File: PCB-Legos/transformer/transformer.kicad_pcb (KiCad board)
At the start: 4 copper layers, 21.8 x 9.7 mm, 3 parts, among them J1 Conn_Coaxial, U1 NCS3-272+

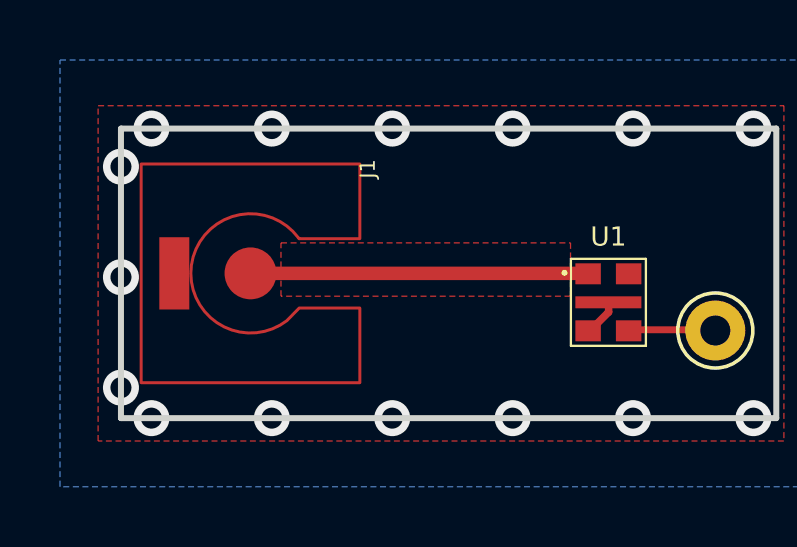
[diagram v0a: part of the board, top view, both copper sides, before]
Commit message: sweaks to sma connector footprint to unbork the errors from the eagle port
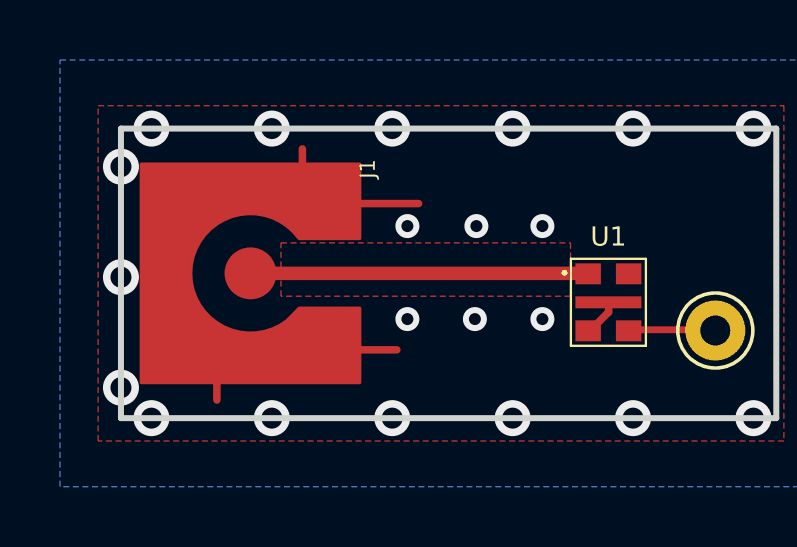
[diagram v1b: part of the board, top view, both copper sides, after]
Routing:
- net GND: track 1.74 -> 10.3 mm, vias 15 -> 21
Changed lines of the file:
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@@
         (xy -3.6449 -3.6449)
         (xy -1.1557 -3.6449)
-      ) (layer "F.Cu") (width 0.1) (fill none))
+      ) (layer "F.Cu") (width 0.1) (fill solid))
     (fp_poly (pts
-        (xy 1.4478 -1.4478)
-        (xy 3.302 -1.4478)
-        (xy 3.302 -3.302)
-        (xy 1.4478 -3.302)
-      ) (layer "F.Paste") (width 0.1) (fill none))
+        (xy -3.81 3.81)
+        (xy -1.205 3.81)
+        (xy -1.27 -3.81)
+        (xy -3.81 -3.81)
+      ) (layer "F.Mask") (width 0.1) (fill solid))
     (fp_poly (pts
-        (xy 1.4478 3.302)
-        (xy 3.302 3.302)
-        (xy 3.302 1.4478)
-        (xy 1.4478 1.4478)
-      ) (layer "F.Paste") (width 0.1) (fill none))
-    (fp_poly (pts
-        (xy -3.302 3.302)
-        (xy -1.4478 3.302)
-        (xy -1.4478 1.4478)
-        (xy -3.302 1.4478)
-      ) (layer "F.Paste") (width 0.1) (fill none))
-    (fp_poly (pts
-        (xy -3.302 -1.4478)
-        (xy -1.4478 -1.4478)
-        (xy -1.4478 -3.302)
-        (xy -3.302 -3.302)
-      ) (layer "F.Paste") (width 0.1) (fill none))
-    (fp_poly (pts
-        (xy -3.429 -0.762)
-        (xy -0.635 -0.762)
-        (xy -0.635 -1.143)
-        (xy -3.429 -1.143)
-      ) (layer "F.Mask") (width 0.1) (fill none))
-    (fp_poly (pts
-        (xy 0.635 -0.762)
-        (xy 3.429 -0.762)
-        (xy 3.429 -1.143)
-        (xy 0.635 -1.143)
-      ) (layer "F.Mask") (width 0.1) (fill none))
-    (fp_poly (pts
-        (xy -3.429 3.429)
-        (xy 3.429 3.429)
-        (xy 3.429 -0.889)
-        (xy -3.429 -0.889)
-      ) (layer "F.Mask") (width 0.1) (fill none))
-    (fp_poly (pts
-        (xy -3.429 -1.016)
-        (xy 3.429 -1.016)
-        (xy 3.429 -3.429)
-        (xy -3.429 -3.429)
-      ) (layer "F.Mask") (width 0.1) (fill none))
-    (fp_poly (pts
-        (xy 0.635 -0.762)
-        (xy 3.429 -0.762)
-        (xy 3.429 -1.143)
-        (xy 0.635 -1.143)
-      ) (layer "F.Mask") (width 0.1) (fill none))
+        (xy 1.27 3.81)
+        (xy 3.81 3.81)
+        (xy 3.81 -3.81)
+        (xy 1.27 -3.81)
+      ) (layer "F.Mask") (width 0.1) (fill solid))
     (fp_line (start -4.1 4.1) (end -4.1 -4.1) (layer "F.CrtYd") (width 0.05))
     (fp_line (start 4.1 -4.1) (end 4.1 4.1) (layer "F.CrtYd") (width 0.05))
@@
     (pad "CENTER" smd roundrect (at 0 0 270) (size 1.73 1.73) (layers "F.Cu" "F.Paste") (roundrect_rratio 0.5)
       (net 1 "Net-(J1-Pad1)") (solder_mask_margin 0.0635))
-    (pad "SHIELD" smd rect (at 0 2.54 270) (size 2.41 1) (layers "F.Cu" "F.Paste" "F.Mask")
-      (net 2 "GND") (solder_mask_margin 0.0635))
   )
   (gr_poly
     (pts
-      (xy 113.538 50.038)
-      (xy 103.886 50.038)
-      (xy 103.886 48.768)
-      (xy 113.538 48.768)
-    ) (layer "F.Mask") (width 0) (fill none))
+      (xy 113.613 50.045)
+      (xy 103.886 50.045)
+      (xy 103.886 48.5)
+      (xy 113.613 48.5)
+    ) (layer "F.Mask") (width 0.1) (fill solid))
   (gr_rect (start 120.396 44.45) (end 98.552 54.102) (layer "Edge.Cuts") (width 0.2) (fill none))
   (segment (start 114.067 49.276) (end 114.133 49.342) (width 0.25) (layer "F.Cu") (net 1))
   (segment (start 103.212 49.276) (end 114.212 49.276) (width 0.45) (layer "F.Cu") (net 1))
   (segment (start 114.808 50.292) (end 114.3 50.292) (width 0.25) (layer "F.Cu") (net 2))
+  (segment (start 101.75 52.025) (end 101.75 53.5) (width 0.25) (layer "F.Cu") (net 2))
   (segment (start 114.808 50.567) (end 114.133 51.242) (width 0.25) (layer "F.Cu") (net 2))
   (segment (start 114.808 50.292) (end 114.808 50.567) (width 0.25) (layer "F.Cu") (net 2))
+  (segment (start 104.6 46.375) (end 104.6 45.125) (width 0.25) (layer "F.Cu") (net 2))
+  (segment (start 105.325 51.825) (end 105.3 51.8) (width 0.25) (layer "F.Cu") (net 2))
+  (segment (start 107.75 51.825) (end 105.325 51.825) (width 0.25) (layer "F.Cu") (net 2))
+  (segment (start 108.475 46.95) (end 105.1 46.95) (width 0.25) (layer "F.Cu") (net 2))
   (via (at 115.6208 54.102) (size 1.2) (drill 0.7) (layers "F.Cu" "B.Cu") (free) (net 2))
+  (via (at 112.6 50.8) (size 0.8) (drill 0.4) (layers "F.Cu" "B.Cu") (free) (net 2))
+  (via (at 112.6 47.7) (size 0.8) (drill 0.4) (layers "F.Cu" "B.Cu") (free) (net 2))
   (via (at 98.552 53.086) (size 1.2) (drill 0.7) (layers "F.Cu" "B.Cu") (free) (net 2))
   (via (at 107.5944 44.45) (size 1.2) (drill 0.7) (layers "F.Cu" "B.Cu") (free) (net 2))
   (via (at 107.5944 54.102) (size 1.2) (drill 0.7) (layers "F.Cu" "B.Cu") (free) (net 2))
   (via (at 111.6076 44.45) (size 1.2) (drill 0.7) (layers "F.Cu" "B.Cu") (free) (net 2))
+  (via (at 108.1 47.7) (size 0.8) (drill 0.4) (layers "F.Cu" "B.Cu") (free) (net 2))
   (via (at 119.634 54.102) (size 1.2) (drill 0.7) (layers "F.Cu" "B.Cu") (free) (net 2))
+  (via (at 108.1 50.8) (size 0.8) (drill 0.4) (layers "F.Cu" "B.Cu") (free) (net 2))
   (via (at 103.5812 44.45) (size 1.2) (drill 0.7) (layers "F.Cu" "B.Cu") (free) (net 2))
   (via (at 99.568 54.102) (size 1.2) (drill 0.7) (layers "F.Cu" "B.Cu") (free) (net 2))
   (via (at 103.5812 54.102) (size 1.2) (drill 0.7) (layers "F.Cu" "B.Cu") (free) (net 2))
+  (via (at 110.35 50.8) (size 0.8) (drill 0.4) (layers "F.Cu" "B.Cu") (free) (net 2))
   (via (at 115.6208 44.45) (size 1.2) (drill 0.7) (layers "F.Cu" "B.Cu") (free) (net 2))
   (via (at 111.6076 54.102) (size 1.2) (drill 0.7) (layers "F.Cu" "B.Cu") (free) (net 2))
@@
   (via (at 98.552 45.72) (size 1.2) (drill 0.7) (layers "F.Cu" "B.Cu") (free) (net 2))
   (via (at 99.568 44.45) (size 1.2) (drill 0.7) (layers "F.Cu" "B.Cu") (net 2))
+  (via (at 110.4 47.7) (size 0.8) (drill 0.4) (layers "F.Cu" "B.Cu") (free) (net 2))
   (segment (start 115.4833 51.1556) (end 118.2983 51.1556) (width 0.23) (layer "F.Cu") (net 3))
   (segment (start 118.298 51.242) (end 118.364 51.308) (width 0.25) (layer "F.Cu") (net 3))

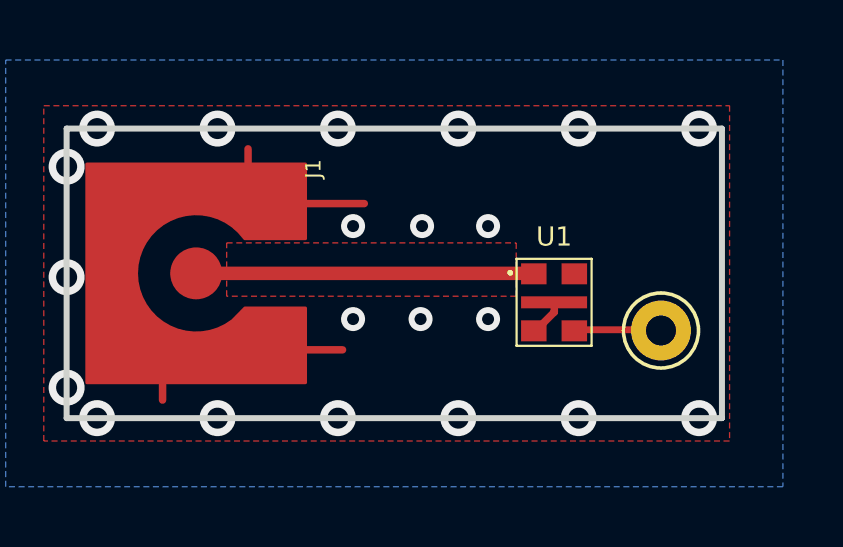
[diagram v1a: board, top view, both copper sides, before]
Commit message: Fixed .gitignore for KiCAD 6, removed backups and other temp files, updated board file with 4 layer oshpark from the oresat-kicad repo, moved antenna much closer to the transformer and reduced the trace size to minimum (as close to 150 ohms as possible), and set net classes to RF-50-MAX which gives lots of ground clearance.
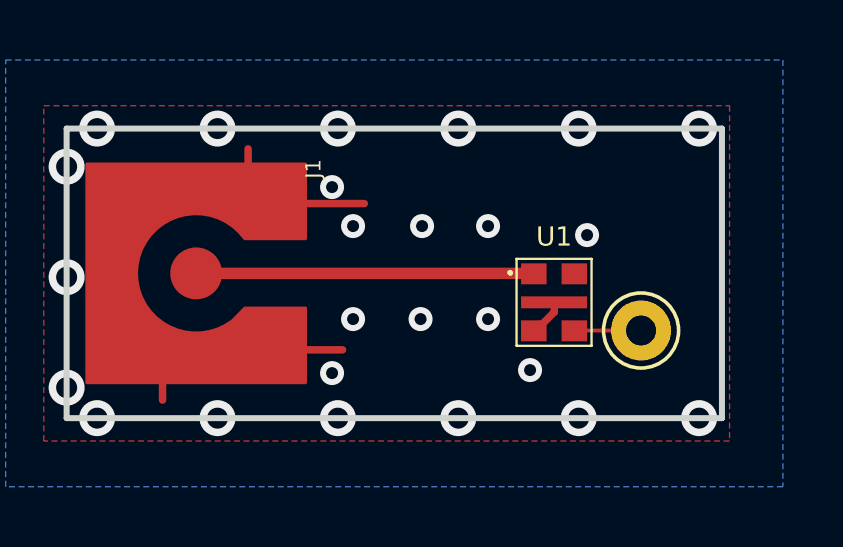
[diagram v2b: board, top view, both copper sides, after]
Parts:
- moved H1 0.66 mm to (117.7, 51.2)
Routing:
- net Net-(H1-Pad1): track 2.91 -> 2.32 mm
- net GND: vias 21 -> 25
- removed copper zone on F.Cu, net (none)
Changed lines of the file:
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@@
   (paper "A4")
   (layers
-    (0 "F.Cu" signal)
+    (0 "F.Cu" jumper)
     (1 "In1.Cu" signal)
     (2 "In2.Cu" signal)
     (31 "B.Cu" signal)
-    (32 "B.Adhes" user "B.Adhesive")
-    (33 "F.Adhes" user "F.Adhesive")
     (34 "B.Paste" user)
     (35 "F.Paste" user)
@@
     (40 "Dwgs.User" user "User.Drawings")
     (41 "Cmts.User" user "User.Comments")
-    (42 "Eco1.User" user "User.Eco1")
-    (43 "Eco2.User" user "User.Eco2")
     (44 "Edge.Cuts" user)
     (45 "Margin" user)
@@
     (48 "B.Fab" user)
     (49 "F.Fab" user)
-    (50 "User.1" user)
-    (51 "User.2" user)
-    (52 "User.3" user)
-    (53 "User.4" user)
-    (54 "User.5" user)
-    (55 "User.6" user)
-    (56 "User.7" user)
-    (57 "User.8" user)
-    (58 "User.9" user)
   )
   (setup
@@
     )
     (pad_to_mask_clearance 0)
+    (solder_mask_min_width 0.1016)
     (pcbplotparams
       (layerselection 0x00010fc_ffffffff)
@@
   (net 3 "Net-(H1-Pad1)")
   (footprint "Connector_Pin:Pin_D1.0mm_L10.0mm" (layer "F.Cu")
-    (at 118.364 51.181)
+    (at 117.7 51.181)
     (descr "solder Pin_ diameter 1.0mm, hole diameter 1.0mm (press fit), length 10.0mm")
     (tags "solder Pin_ press fit")
@@
       (net 1 "Net-(J1-Pad1)") (solder_mask_margin 0.0635))
   )
-  (gr_poly
-    (pts
-      (xy 113.613 50.045)
-      (xy 103.886 50.045)
-      (xy 103.886 48.5)
-      (xy 113.613 48.5)
-    ) (layer "F.Mask") (width 0.1) (fill solid))
   (gr_rect (start 120.396 44.45) (end 98.552 54.102) (layer "Edge.Cuts") (width 0.2) (fill none))
   (segment (start 114.067 49.276) (end 114.133 49.342) (width 0.25) (layer "F.Cu") (net 1))
-  (segment (start 103.212 49.276) (end 114.212 49.276) (width 0.45) (layer "F.Cu") (net 1))
+  (segment (start 103.212 49.276) (end 114.212 49.276) (width 0.38) (layer "F.Cu") (net 1))
   (segment (start 114.808 50.292) (end 114.3 50.292) (width 0.25) (layer "F.Cu") (net 2))
   (segment (start 101.75 52.025) (end 101.75 53.5) (width 0.25) (layer "F.Cu") (net 2))
@@
   (segment (start 107.75 51.825) (end 105.325 51.825) (width 0.25) (layer "F.Cu") (net 2))
   (segment (start 108.475 46.95) (end 105.1 46.95) (width 0.25) (layer "F.Cu") (net 2))
+  (via (at 114 52.5) (size 0.8) (drill 0.4) (layers "F.Cu" "B.Cu") (free) (net 2))
+  (via (at 115.9 48) (size 0.8) (drill 0.4) (layers "F.Cu" "B.Cu") (free) (net 2))
+  (via (at 107.4 46.4) (size 0.8) (drill 0.4) (layers "F.Cu" "B.Cu") (free) (net 2))
   (via (at 115.6208 54.102) (size 1.2) (drill 0.7) (layers "F.Cu" "B.Cu") (free) (net 2))
   (via (at 112.6 50.8) (size 0.8) (drill 0.4) (layers "F.Cu" "B.Cu") (free) (net 2))
@@
   (via (at 111.6076 44.45) (size 1.2) (drill 0.7) (layers "F.Cu" "B.Cu") (free) (net 2))
   (via (at 108.1 47.7) (size 0.8) (drill 0.4) (layers "F.Cu" "B.Cu") (free) (net 2))
+  (via (at 107.4 52.6) (size 0.8) (drill 0.4) (layers "F.Cu" "B.Cu") (free) (net 2))
   (via (at 119.634 54.102) (size 1.2) (drill 0.7) (layers "F.Cu" "B.Cu") (free) (net 2))
   (via (at 108.1 50.8) (size 0.8) (drill 0.4) (layers "F.Cu" "B.Cu") (free) (net 2))
@@
   (via (at 99.568 44.45) (size 1.2) (drill 0.7) (layers "F.Cu" "B.Cu") (net 2))
   (via (at 110.4 47.7) (size 0.8) (drill 0.4) (layers "F.Cu" "B.Cu") (free) (net 2))
-  (segment (start 115.4833 51.1556) (end 118.2983 51.1556) (width 0.23) (layer "F.Cu") (net 3))
+  (segment (start 115.4851 51.181) (end 115.4749 51.1912) (width 0.127) (layer "F.Cu") (net 3))
   (segment (start 118.298 51.242) (end 118.364 51.308) (width 0.25) (layer "F.Cu") (net 3))
-  (zone (net 0) (net_name "") (layer "F.Cu") (hatch edge 0.508)
-    (connect_pads (clearance 0.381))
-    (min_thickness 0.254) (filled_areas_thickness no)
-    (fill yes (thermal_gap 0.508) (thermal_bridge_width 0.508))
-    (polygon
-      (pts
-        (xy 113.538 50.038)
-        (xy 103.886 50.038)
-        (xy 103.886 48.26)
-        (xy 113.538 48.26)
-      )
-    )
-  )
+  (segment (start 117.7 51.181) (end 115.4851 51.181) (width 0.127) (layer "F.Cu") (net 3))
   (zone (net 2) (net_name "GND") (layer "F.Cu") (hatch edge 0.508)
     (connect_pads (clearance 0.381))
@@
       )
     )
+  )
+  (zone (net 0) (net_name "") (layer "F.Mask") (hatch full 0.508)
+    (connect_pads (clearance 0.381))
+    (min_thickness 0.127) (filled_areas_thickness no)
+    (fill yes (thermal_gap 0.508) (thermal_bridge_width 0.508))
+    (polygon
+      (pts
+        (xy 113.4 50.3)
+        (xy 103.9 50.3)
+        (xy 103.9 48.2)
+        (xy 113.4 48.2)
+      )
+    )

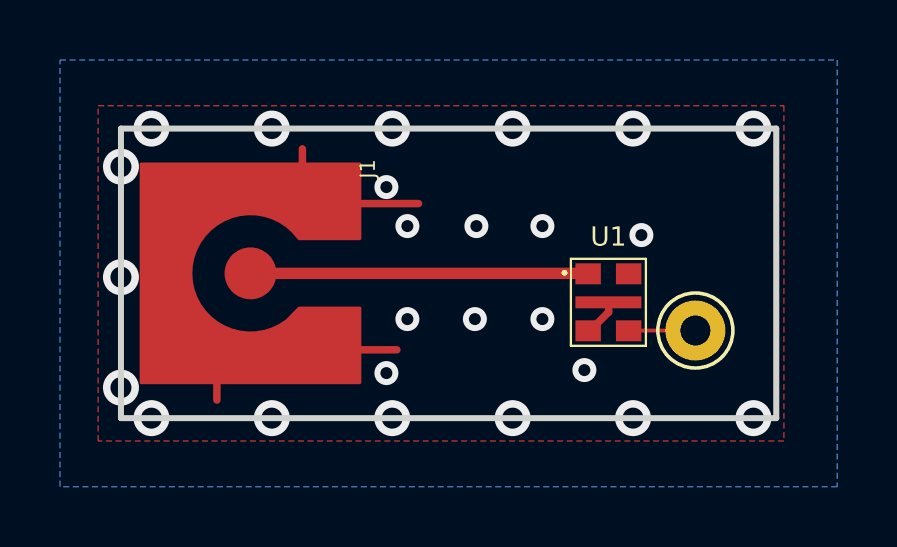
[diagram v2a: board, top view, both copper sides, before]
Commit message: fixed SMA connector footprint, moved text from paste to silk layer
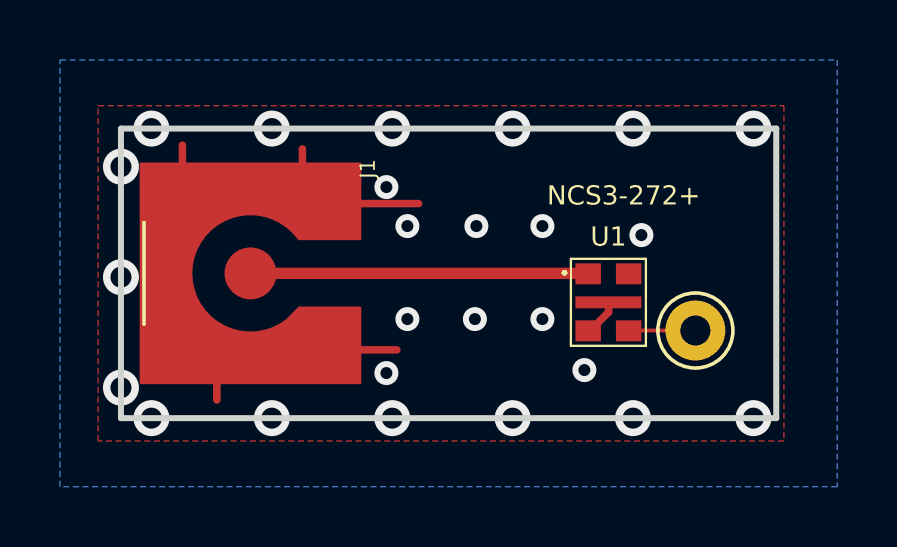
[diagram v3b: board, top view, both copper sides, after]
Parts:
- J1: footprint HGS_Reflector:132134-10 -> Footprints:J-Amphenol-132134-10-SMA-F-SMT-vertical
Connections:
- J1 pad CENTER: Net-(J1-Pad1) -> (no net)
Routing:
- net (no net): track 0.00 -> 0.90 mm
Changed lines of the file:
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@@
       (effects (font (size 0.640777 0.640777) (thickness 0.15)))
     )
-    (fp_text value "NCS3-272+" (at 0.508 -3.556) (layer "F.Paste")
+    (fp_text value "NCS3-272+" (at 0.508 -3.556) (layer "F.SilkS")
       (effects (font (size 0.640436 0.640436) (thickness 0.15)))
     )
@@
     (pad "6" smd rect locked (at 0.675 -0.95) (size 0.85 0.7) (layers "F.Cu" "F.Paste" "F.Mask"))
   )
-  (footprint "HGS_Reflector:132134-10" (layer "F.Cu")
+  (footprint "Footprints:J-Amphenol-132134-10-SMA-F-SMT-vertical" (layer "F.Cu")
     (at 102.87 49.276 -90)
     (property "Sheetfile" "transformer.kicad_sch")
@@
       ) (layer "F.Cu") (width 0.1) (fill solid))
     (fp_poly (pts
+        (xy -3.5 -1.6)
+        (xy -1.6458 -1.6)
+        (xy -1.6458 -3.4542)
+        (xy -3.5 -3.4542)
+      ) (layer "F.Paste") (width 0.1) (fill solid))
+    (fp_poly (pts
+        (xy -3.53 3.45)
+        (xy -1.6758 3.45)
+        (xy -1.6758 1.5958)
+        (xy -3.53 1.5958)
+      ) (layer "F.Paste") (width 0.1) (fill solid))
+    (fp_poly (pts
+        (xy 1.57 -1.6)
+        (xy 3.4242 -1.6)
+        (xy 3.4242 -3.4542)
+        (xy 1.57 -3.4542)
+      ) (layer "F.Paste") (width 0.1) (fill solid))
+    (fp_poly (pts
+        (xy 1.57 3.4)
+        (xy 3.4242 3.4)
+        (xy 3.4242 1.5458)
+        (xy 1.57 1.5458)
+      ) (layer "F.Paste") (width 0.1) (fill solid))
+    (fp_line (start -1.7 3.55) (end 1.7 3.55) (layer "F.SilkS") (width 0.12))
+    (fp_poly (pts
         (xy -3.81 3.81)
         (xy -1.205 3.81)
@@
       ) (layer "F.Mask") (width 0.1) (fill solid))
     (fp_line (start -4.1 4.1) (end -4.1 -4.1) (layer "F.CrtYd") (width 0.05))
+    (fp_line (start -4.1 -4.1) (end 4.1 -4.1) (layer "F.CrtYd") (width 0.05))
     (fp_line (start 4.1 -4.1) (end 4.1 4.1) (layer "F.CrtYd") (width 0.05))
-    (fp_line (start -4.1 -4.1) (end 4.1 -4.1) (layer "F.CrtYd") (width 0.05))
     (fp_line (start 4.1 4.1) (end -4.1 4.1) (layer "F.CrtYd") (width 0.05))
+    (fp_line (start -3.175 2.675) (end -3.175 -2.675) (layer "F.Fab") (width 0.127))
+    (fp_line (start 3.175 -2.675) (end 3.175 2.675) (layer "F.Fab") (width 0.127))
     (fp_line (start 2.675 3.175) (end -2.675 3.175) (layer "F.Fab") (width 0.127))
     (fp_line (start -2.675 -3.175) (end 2.675 -3.175) (layer "F.Fab") (width 0.127))
-    (fp_line (start -3.175 2.675) (end -3.175 -2.675) (layer "F.Fab") (width 0.127))
-    (fp_line (start 3.175 -2.675) (end 3.175 2.675) (layer "F.Fab") (width 0.127))
-    (fp_arc (start 2.675 -3.175) (mid 3.028553 -3.028553) (end 3.175 -2.675) (layer "F.Fab") (width 0.127))
-    (fp_arc (start -2.675 3.175) (mid -3.028553 3.028553) (end -3.175 2.675) (layer "F.Fab") (width 0.127))
     (fp_arc (start -3.175 -2.675) (mid -3.028553 -3.028553) (end -2.675 -3.175) (layer "F.Fab") (width 0.127))
     (fp_arc (start 3.175 2.675) (mid 3.028553 3.028553) (end 2.675 3.175) (layer "F.Fab") (width 0.127))
+    (fp_arc (start -2.675 3.175) (mid -3.028553 3.028553) (end -3.175 2.675) (layer "F.Fab") (width 0.127))
+    (fp_arc (start 2.675 -3.175) (mid 3.028553 -3.028553) (end 3.175 -2.675) (layer "F.Fab") (width 0.127))
     (fp_circle (center 0 0) (end 3.175 0) (layer "F.Fab") (width 0.127) (fill none))
-    (pad "CENTER" smd roundrect (at 0 0 270) (size 1.73 1.73) (layers "F.Cu" "F.Paste") (roundrect_rratio 0.5)
-      (net 1 "Net-(J1-Pad1)") (solder_mask_margin 0.0635))
+    (pad "CENTER" smd roundrect (at 0 0 270) (size 1.73 1.73) (layers "F.Cu" "F.Paste" "F.Mask") (roundrect_rratio 0.5)
+      (solder_mask_margin 0.0635))
   )
   (gr_rect (start 120.396 44.45) (end 98.552 54.102) (layer "Edge.Cuts") (width 0.2) (fill none))
+  (segment (start 100.6 45) (end 100.6 45.9) (width 0.25) (layer "F.Cu") (net 0))
   (segment (start 114.067 49.276) (end 114.133 49.342) (width 0.25) (layer "F.Cu") (net 1))
   (segment (start 103.212 49.276) (end 114.212 49.276) (width 0.38) (layer "F.Cu") (net 1))
